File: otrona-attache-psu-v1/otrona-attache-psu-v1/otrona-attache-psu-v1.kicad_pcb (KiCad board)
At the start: 2 copper layers, 90.1 x 103 mm, 30 parts, among them J1 VIDEO, J10 HSYNC, J11 VSYNC, J12 VIDEO, J13 SPK_GND, J14 SPK_AUDIO, J15 ATX_POK, J16 5V, J17 GND, J18 GND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

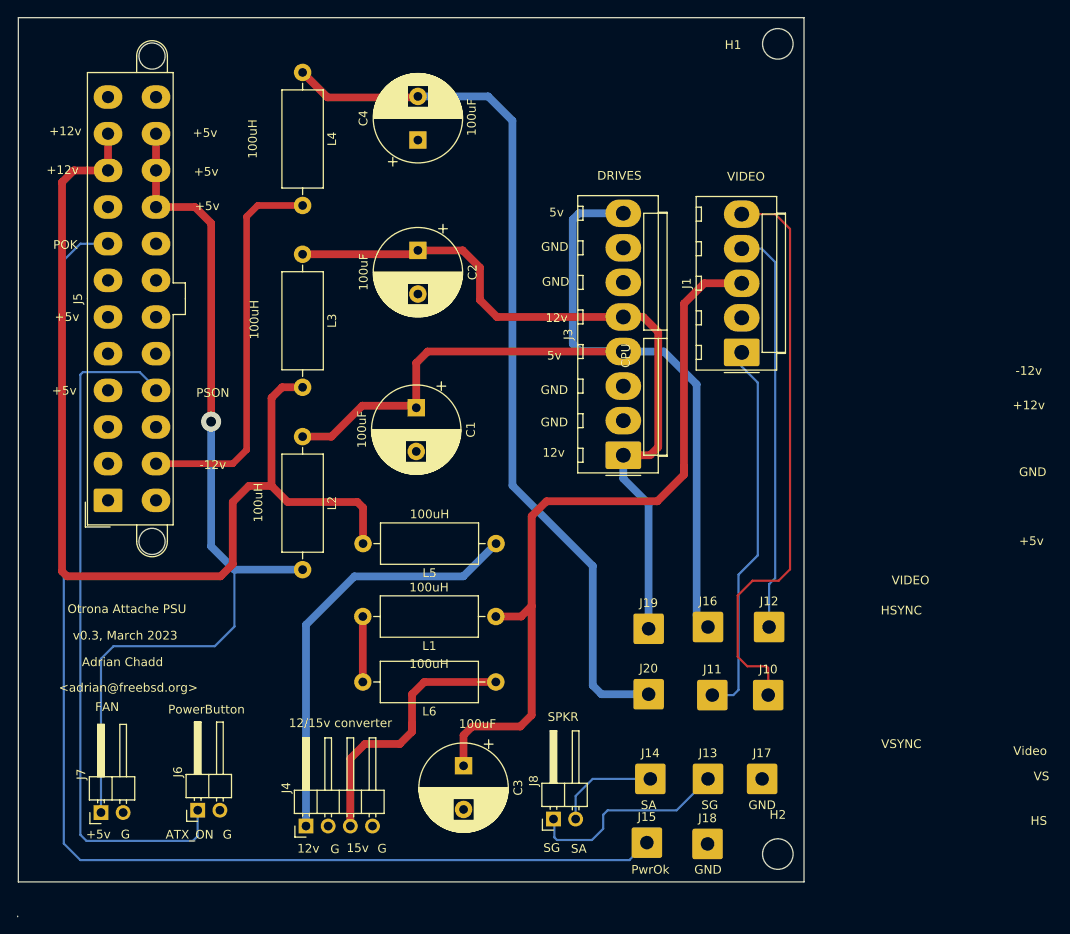
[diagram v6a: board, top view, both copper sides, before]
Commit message: more layout changes, ground plane
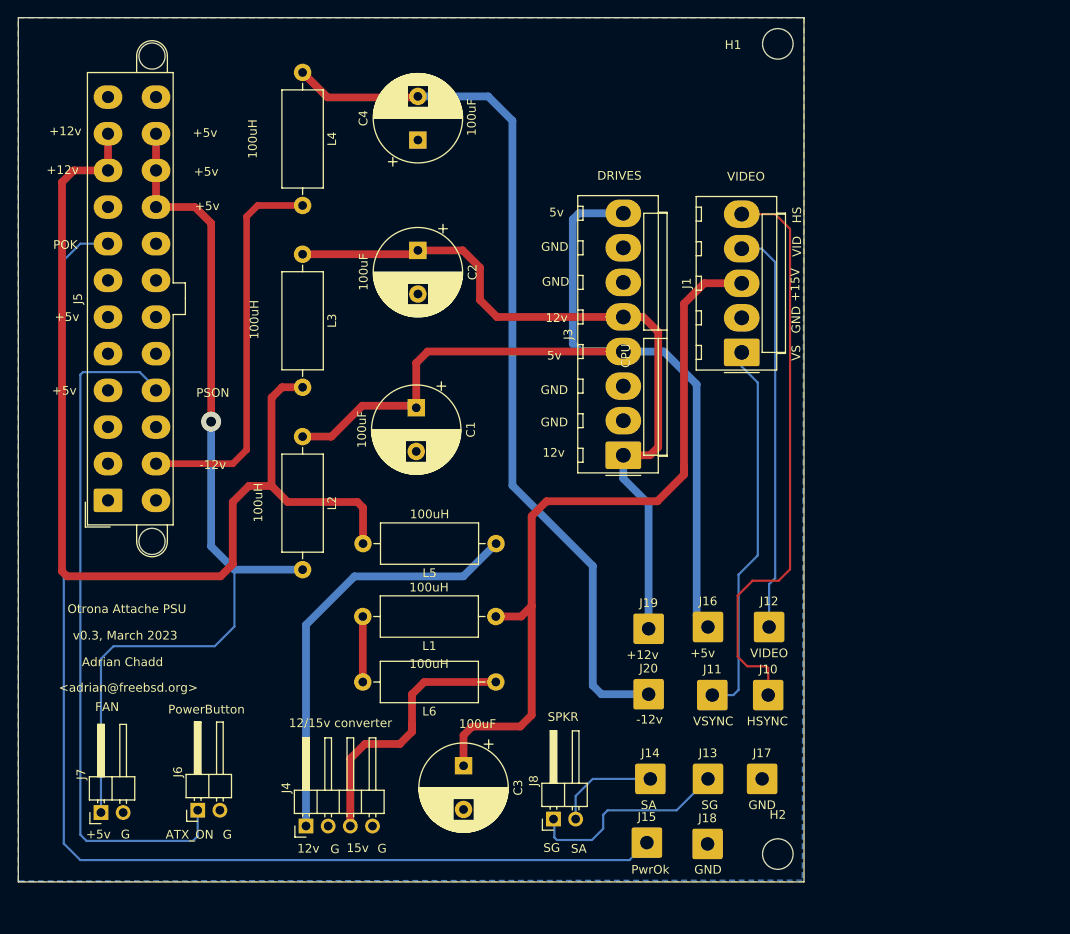
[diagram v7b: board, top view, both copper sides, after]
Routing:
- added copper zone on B.Cu, net GND
- added copper zone on F.Cu, net GND
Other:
- board size 90.1 x 103 mm -> 90 x 99 mm
- board text added: "+15V"
- board text added: "VID"
- board text removed: "Video"
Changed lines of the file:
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@@
     )
+  )
+  (gr_text +15V (at 104 45.6 90) (layer F.SilkS)
+    (effects (font (size 1 1) (thickness 0.15)))
+  )
+  (gr_text VID (at 104.2 41.2 90) (layer F.SilkS)
+    (effects (font (size 1 1) (thickness 0.15)))
   )
   (dimension 99.99472 (width 0.15) (layer Dwgs.User)
@@
     (effects (font (size 1 1) (thickness 0.15)))
   )
-  (gr_text HS (at 131.9 107) (layer F.SilkS)
-    (effects (font (size 1 1) (thickness 0.15)))
-  )
-  (gr_text VS (at 132.2 101.9) (layer F.SilkS)
-    (effects (font (size 1 1) (thickness 0.15)))
-  )
-  (gr_text Video (at 130.9 99) (layer F.SilkS)
+  (gr_text HS (at 104.2 37.6 90) (layer F.SilkS)
+    (effects (font (size 1 1) (thickness 0.15)))
+  )
+  (gr_text VS (at 104.1 53.4 90) (layer F.SilkS)
     (effects (font (size 1 1) (thickness 0.15)))
   )
@@
     (effects (font (size 1 1) (thickness 0.15)))
   )
-  (gr_text +5v (at 131.05 74.95) (layer F.SilkS)
-    (effects (font (size 1 1) (thickness 0.15)))
-  )
-  (gr_text GND (at 131.2 67.05) (layer F.SilkS)
+  (gr_text +5v (at 93.4 87.8) (layer F.SilkS)
+    (effects (font (size 1 1) (thickness 0.15)))
+  )
+  (gr_text GND (at 104.1 49.6 90) (layer F.SilkS)
     (effects (font (size 1 1) (thickness 0.15)))
   )
@@
     (effects (font (size 1 1) (thickness 0.15)))
   )
-  (gr_text +12v (at 130.75 59.4) (layer F.SilkS)
-    (effects (font (size 1 1) (thickness 0.15)))
-  )
-  (gr_text -12v (at 130.75 55.45) (layer F.SilkS)
+  (gr_text +12v (at 86.5 88) (layer F.SilkS)
+    (effects (font (size 1 1) (thickness 0.15)))
+  )
+  (gr_text -12v (at 87.3 95.4) (layer F.SilkS)
     (effects (font (size 1 1) (thickness 0.15)))
   )
@@
     (effects (font (size 1 1) (thickness 0.15)))
   )
-  (gr_text VSYNC (at 116.15 98.2) (layer F.SilkS)
+  (gr_text VSYNC (at 94.6 95.6) (layer F.SilkS)
     (effects (font (size 1 1) (thickness 0.15)))
   )
@@
     (effects (font (size 1 1) (thickness 0.15)))
   )
-  (gr_text "VIDEO\n" (at 117.2 79.45) (layer F.SilkS)
-    (effects (font (size 1 1) (thickness 0.15)))
-  )
-  (gr_text "HSYNC\n" (at 116.15 82.9) (layer F.SilkS)
+  (gr_text "VIDEO\n" (at 101 87.8) (layer F.SilkS)
+    (effects (font (size 1 1) (thickness 0.15)))
+  )
+  (gr_text "HSYNC\n" (at 100.8 95.6) (layer F.SilkS)
     (effects (font (size 1 1) (thickness 0.15)))
   )
@@
   )
   (gr_line (start 15 15) (end 15 114) (layer Edge.Cuts) (width 0.05))
-  (gr_line (start 14.9225 117.983) (end 14.9225 117.9195) (layer Edge.Cuts) (width 0.05))
   (gr_line (start 15 114) (end 105 114) (layer Edge.Cuts) (width 0.05))
   (gr_line (start 15 15) (end 105 15) (layer Edge.Cuts) (width 0.05))
@@
   (segment (start 35 109.3) (end 35.54606 108.75394) (width 0.25) (layer B.Cu) (net 19))
   (segment (start 54.46 83.6) (end 54.46 91.1) (width 0.889) (layer F.Cu) (net 21))
+  (zone (net 1) (net_name GND) (layer B.Cu) (hatch edge 0.508)
+    (connect_pads (clearance 0.508))
+    (min_thickness 0.254)
+    (fill yes (arc_segments 32) (thermal_gap 0.508) (thermal_bridge_width 0.508))
+    (polygon
+      (pts
+        (xy 104.8 113.8) (xy 15 113.9) (xy 15 15) (xy 105 15)
+      )
+    )
+  )
+  (zone (net 1) (net_name GND) (layer F.Cu) (hatch edge 0.508)
+    (connect_pads (clearance 0.508))
+    (min_thickness 0.254)
+    (fill yes (arc_segments 32) (thermal_gap 0.508) (thermal_bridge_width 0.508))
+    (polygon
+      (pts
+        (xy 105 114) (xy 15 114) (xy 15 15) (xy 105 15)
+      )
+    )
+  )
 )

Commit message: Change the version, ha
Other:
- board text added: "v0.4, December 2023"
- board text removed: "v0.3, March 2023"
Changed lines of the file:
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@@
   (page A4)
   (layers
-    (0 F.Cu signal)
-    (31 B.Cu signal)
+    (0 F.Cu signal hide)
+    (31 B.Cu signal hide)
     (32 B.Adhes user)
     (33 F.Adhes user)
@@
     (effects (font (size 1 1) (thickness 0.15)))
   )
-  (gr_text "v0.3, March 2023" (at 27.23636 85.77594) (layer F.SilkS)
+  (gr_text "v0.4, December 2023" (at 27.23636 85.77594) (layer F.SilkS)
     (effects (font (size 1 1) (thickness 0.15)))
   )
